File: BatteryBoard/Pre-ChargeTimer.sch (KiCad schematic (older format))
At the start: 9 parts

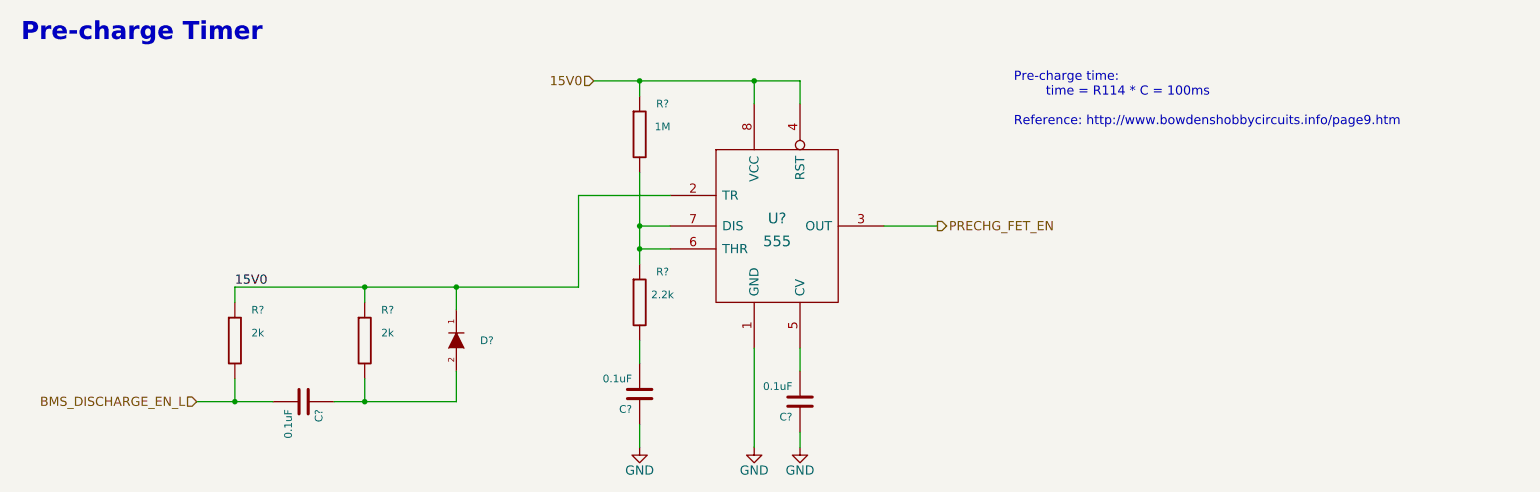
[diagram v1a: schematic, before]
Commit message: Added footprints for most components; started layout
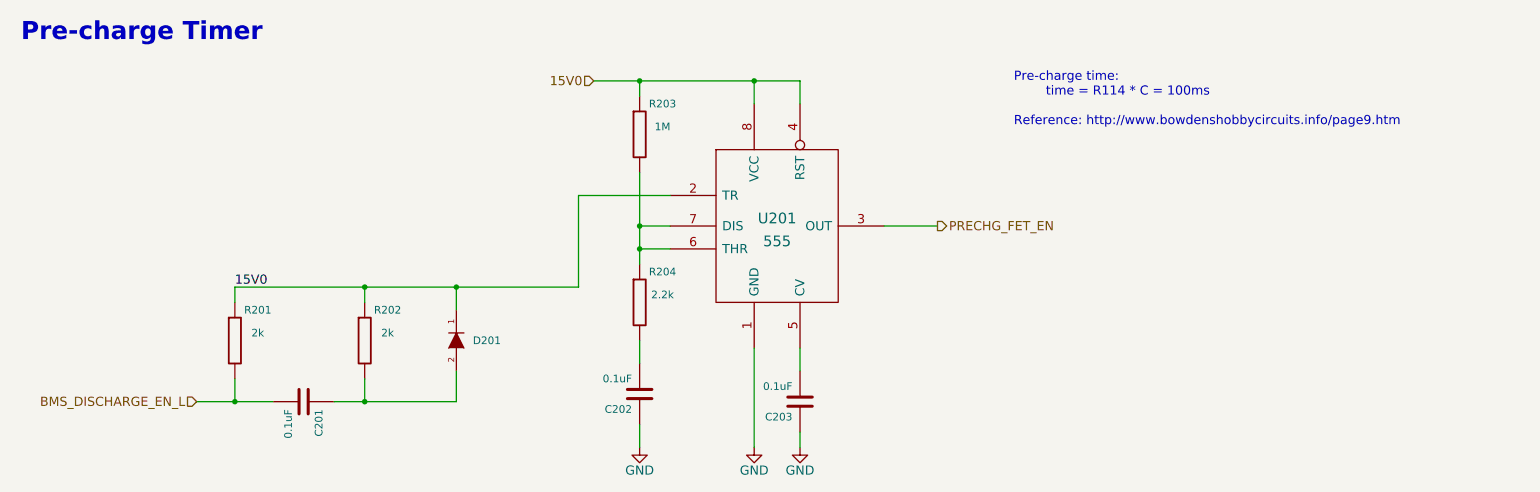
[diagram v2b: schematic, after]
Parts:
- C201, C202, C203: renamed from C?; footprint (none) -> Capacitors_SMD:C_0805_HandSoldering
- D201: renamed from D?; footprint (none) -> Diodes_SMD:D_SOD-523; Digi-Key PN (none) -> 1N4148XTPMSCT-ND; Mfg. (none) -> Micro; Mfg. PN (none) -> 1N4148X-TP
- R201, R202, R203, R204: renamed from R?; footprint (none) -> Resistors_SMD:R_0805_HandSoldering
- U201: renamed from U?; footprint (none) -> Housings_SOIC:SOIC-8_3.9x4.9mm_Pitch1.27mm; Digi-Key PN (none) -> 296-14635-1-ND; Mfg. (none) -> Texas Instruments; Mfg. PN (none) -> SA555DR
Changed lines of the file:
@@
 LIBS:xilinx
 LIBS:555
-LIBS:lt3014b
+LIBS:lt3060
+LIBS:lm321_5pin
 LIBS:BatteryBoard-cache
 EELAYER 25 0
@@
 Pre-charge time:\n		time = R114 * C = 100ms\n\nReference: http://www.bowdenshobbycircuits.info/page9.htm
 $Comp
-L R R?
+L R R201
 U 1 1 59655F30
 P 2050 2750
-F 0 "R?" H 2200 2950 50  0000 C CNN
+F 0 "R201" H 2200 2950 50  0000 C CNN
 F 1 "2k" H 2200 2800 50  0000 C CNN
-F 2 "" V 1980 2750 30  0000 C CNN
+F 2 "Resistors_SMD:R_0805_HandSoldering" V 1980 2750 30  0001 C CNN
 F 3 "" H 2050 2750 30  0000 C CNN
 	1    2050 2750
@@
 15V0
 $Comp
-L C C?
+L C C201
 U 1 1 59655F3C
 P 2500 3150
-F 0 "C?" H 2550 3250 50  0000 L CNN
+F 0 "C201" H 2550 3250 50  0000 L CNN
 F 1 "0.1uF" H 2550 3050 50  0000 L CNN
-F 2 "" H 2538 3000 30  0000 C CNN
+F 2 "Capacitors_SMD:C_0805_HandSoldering" H 2538 3000 30  0001 C CNN
 F 3 "" H 2500 3150 60  0000 C CNN
 	1    2500 3150
@@
 	2700 3150 3500 3150
 $Comp
-L R R?
+L R R202
 U 1 1 59655F45
 P 2900 2750
-F 0 "R?" H 3050 2950 50  0000 C CNN
+F 0 "R202" H 3050 2950 50  0000 C CNN
 F 1 "2k" H 3050 2800 50  0000 C CNN
-F 2 "" V 2830 2750 30  0000 C CNN
+F 2 "Resistors_SMD:R_0805_HandSoldering" V 2830 2750 30  0001 C CNN
 F 3 "" H 2900 2750 30  0000 C CNN
 	1    2900 2750
@@
 $EndComp
 $Comp
-L DIODE D?
+L DIODE D201
 U 1 1 59655F4C
 P 3500 2750
-F 0 "D?" V 3500 2950 50  0000 C CNN
+F 0 "D201" V 3500 2950 50  0000 C CNN
 F 1 "DIODE" H 3500 2650 50  0001 C CNN
-F 2 "" H 3500 2750 60  0000 C CNN
+F 2 "Diodes_SMD:D_SOD-523" H 3500 2750 60  0001 C CNN
 F 3 "" H 3500 2750 60  0000 C CNN
+F 4 "Micro" V 3500 2750 60  0001 C CNN "Mfg."
+F 5 "1N4148X-TP" V 3500 2750 60  0001 C CNN "Mfg. PN"
+F 6 "1N4148XTPMSCT-ND" V 3500 2750 60  0001 C CNN "Digi-Key PN"
 	1    3500 2750
 	0    1    -1   0
@@
 Connection ~ 5450 1050
 $Comp
-L C C?
+L C C203
 U 1 1 59655F5C
 P 5750 3150
-F 0 "C?" H 5800 3250 50  0000 L CNN
+F 0 "C203" H 5800 3250 50  0000 L CNN
 F 1 "0.1uF" H 5800 3050 50  0000 L CNN
-F 2 "" H 5788 3000 30  0000 C CNN
+F 2 "Capacitors_SMD:C_0805_HandSoldering" H 5788 3000 30  0001 C CNN
 F 3 "" H 5750 3150 60  0000 C CNN
 	1    5750 3150
@@
 	5750 3350 5750 3450
 $Comp
-L GND #PWR?
+L GND #PWR203
 U 1 1 59655F65
 P 5750 3450
-F 0 "#PWR?" H 5750 3200 60  0001 C CNN
+F 0 "#PWR203" H 5750 3200 60  0001 C CNN
 F 1 "GND" H 5750 3300 60  0000 C CNN
 F 2 "" H 5750 3450 60  0000 C CNN
@@
 	5450 2800 5450 3450
 $Comp
-L GND #PWR?
+L GND #PWR202
 U 1 1 59655F6C
 P 5450 3450
-F 0 "#PWR?" H 5450 3200 60  0001 C CNN
+F 0 "#PWR202" H 5450 3200 60  0001 C CNN
 F 1 "GND" H 5450 3300 60  0000 C CNN
 F 2 "" H 5450 3450 60  0000 C CNN
@@
 $EndComp
 $Comp
-L R R?
+L R R203
 U 1 1 59655F72
 P 4700 1400
-F 0 "R?" H 4850 1600 50  0000 C CNN
+F 0 "R203" H 4850 1600 50  0000 C CNN
 F 1 "1M" H 4850 1450 50  0000 C CNN
-F 2 "" V 4630 1400 30  0000 C CNN
+F 2 "Resistors_SMD:R_0805_HandSoldering" V 4630 1400 30  0001 C CNN
 F 3 "" H 4700 1400 30  0000 C CNN
 	1    4700 1400
@@
 Connection ~ 4700 2150
 $Comp
-L R R?
+L R R204
 U 1 1 59655F81
 P 4700 2500
-F 0 "R?" H 4850 2700 50  0000 C CNN
+F 0 "R204" H 4850 2700 50  0000 C CNN
 F 1 "2.2k" H 4850 2550 50  0000 C CNN
-F 2 "" V 4630 2500 30  0000 C CNN
+F 2 "Resistors_SMD:R_0805_HandSoldering" V 4630 2500 30  0001 C CNN
 F 3 "" H 4700 2500 30  0000 C CNN
 	1    4700 2500
@@
 $EndComp
 $Comp
-L C C?
+L C C202
 U 1 1 59655F88
 P 4700 3100
-F 0 "C?" H 4750 3200 50  0000 L CNN
+F 0 "C202" H 4750 3200 50  0000 L CNN
 F 1 "0.1uF" H 4750 3000 50  0000 L CNN
-F 2 "" H 4738 2950 30  0000 C CNN
+F 2 "Capacitors_SMD:C_0805_HandSoldering" H 4738 2950 30  0001 C CNN
 F 3 "" H 4700 3100 60  0000 C CNN
 	1    4700 3100
@@
 	4700 3300 4700 3450
 $Comp
-L GND #PWR?
+L GND #PWR201
 U 1 1 59655F91
 P 4700 3450
-F 0 "#PWR?" H 4700 3200 60  0001 C CNN
+F 0 "#PWR201" H 4700 3200 60  0001 C CNN
 F 1 "GND" H 4700 3300 60  0000 C CNN
 F 2 "" H 4700 3450 60  0000 C CNN
@@
 	3500 3150 3500 2950
 $Comp
-L 555 U?
+L 555 U201
 U 1 1 59655F28
 P 5600 2000
-F 0 "U?" H 5600 2050 70  0000 C CNN
+F 0 "U201" H 5600 2050 70  0000 C CNN
 F 1 "555" H 5600 1900 70  0000 C CNN
-F 2 "" H 5600 2000 60  0000 C CNN
+F 2 "Housings_SOIC:SOIC-8_3.9x4.9mm_Pitch1.27mm" H 5600 2000 60  0001 C CNN
 F 3 "" H 5600 2000 60  0000 C CNN
+F 4 "Texas Instruments" H 5600 2000 60  0001 C CNN "Mfg."
+F 5 "SA555DR" H 5600 2000 60  0001 C CNN "Mfg. PN"
+F 6 "296-14635-1-ND" H 5600 2000 60  0001 C CNN "Digi-Key PN"
 	1    5600 2000
 	1    0    0    -1

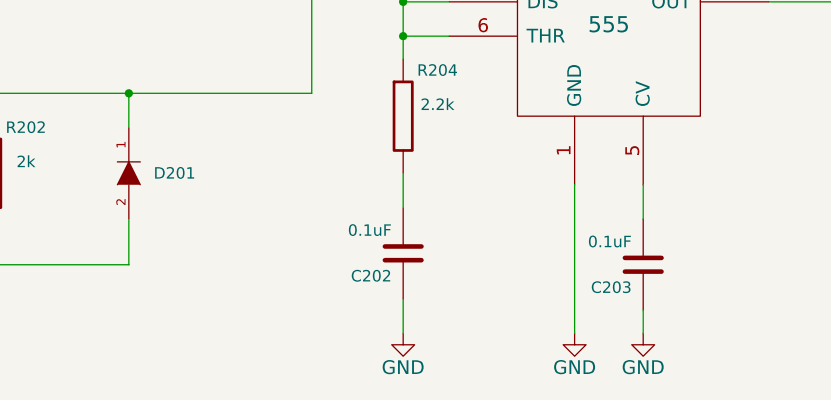
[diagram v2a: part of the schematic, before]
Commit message: Finished adding footprints; roughly placed all components
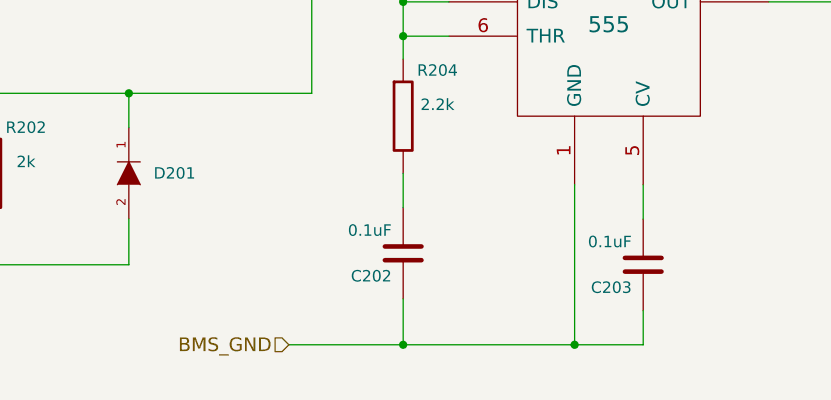
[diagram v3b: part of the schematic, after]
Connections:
- net GND renamed BMS_GND
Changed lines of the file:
@@
 LIBS:lt3060
 LIBS:lm321_5pin
+LIBS:AOB290L_nfet
 LIBS:BatteryBoard-cache
 EELAYER 25 0
@@
 	5750 2950 5750 2800
 Wire Wire Line
-	5750 3350 5750 3450
-$Comp
-L GND #PWR203
-U 1 1 59655F65
-P 5750 3450
-F 0 "#PWR203" H 5750 3200 60  0001 C CNN
-F 1 "GND" H 5750 3300 60  0000 C CNN
-F 2 "" H 5750 3450 60  0000 C CNN
-F 3 "" H 5750 3450 60  0000 C CNN
-	1    5750 3450
-	1    0    0    -1
-$EndComp
+	5750 3500 5750 3350
 Wire Wire Line
-	5450 2800 5450 3450
-$Comp
-L GND #PWR202
-U 1 1 59655F6C
-P 5450 3450
-F 0 "#PWR202" H 5450 3200 60  0001 C CNN
-F 1 "GND" H 5450 3300 60  0000 C CNN
-F 2 "" H 5450 3450 60  0000 C CNN
-F 3 "" H 5450 3450 60  0000 C CNN
-	1    5450 3450
-	1    0    0    -1
-$EndComp
+	5450 3500 5450 2800
 $Comp
 L R R203
@@
 	4700 2900 4700 2750
 Wire Wire Line
-	4700 3300 4700 3450
-$Comp
-L GND #PWR201
-U 1 1 59655F91
-P 4700 3450
-F 0 "#PWR201" H 4700 3200 60  0001 C CNN
-F 1 "GND" H 4700 3300 60  0000 C CNN
-F 2 "" H 4700 3450 60  0000 C CNN
-F 3 "" H 4700 3450 60  0000 C CNN
-	1    4700 3450
-	1    0    0    -1
-$EndComp
+	4700 3300 4700 3500
 Wire Wire Line
 	3500 2550 3500 2400
@@
 Wire Wire Line
 	6300 2000 6650 2000
+Text HLabel 4200 3500 0    60   Input ~ 0
+BMS_GND
+Wire Wire Line
+	4200 3500 5750 3500
+Connection ~ 4700 3500
+Connection ~ 5450 3500
 $EndSCHEMATC

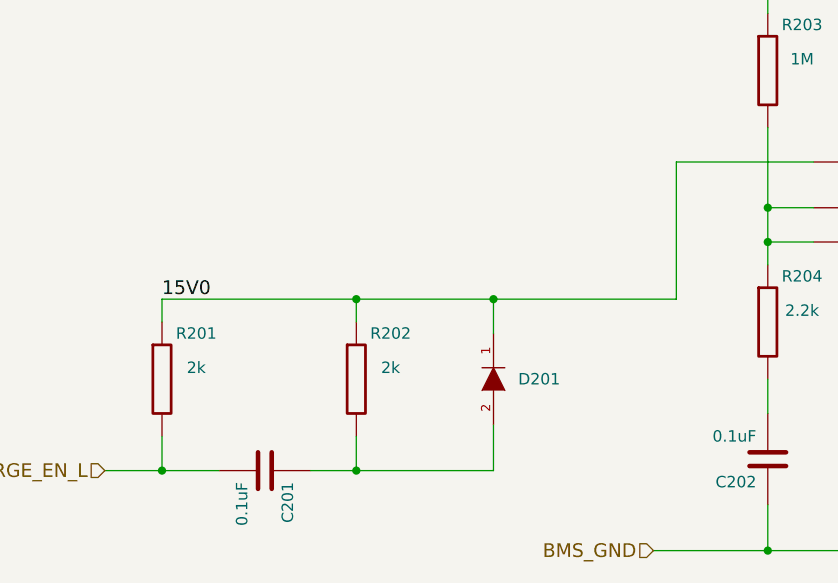
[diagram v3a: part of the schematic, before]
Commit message: Completed layout first pass - ready for review (pending validation w/ simulation)
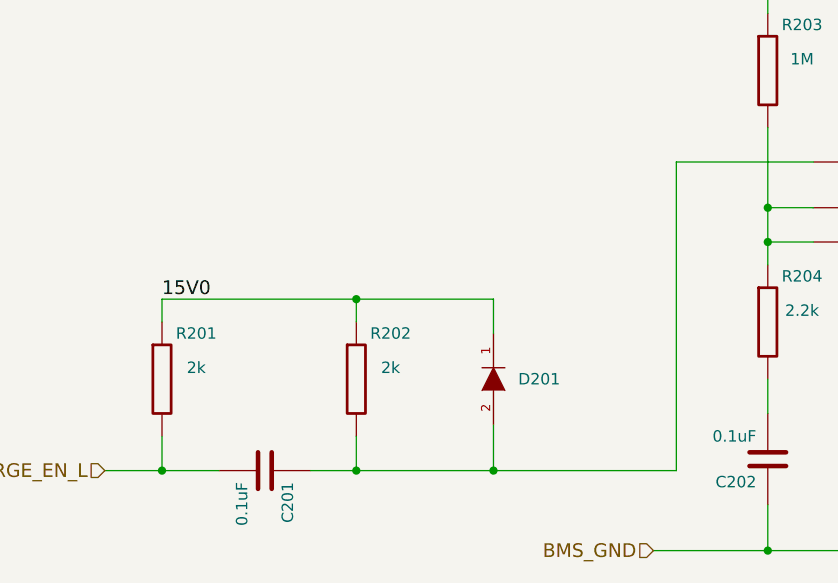
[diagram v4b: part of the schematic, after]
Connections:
- net 15V0: no longer U201.2 (TR)
- net at C201.1, D201.2 (A), R202.2: now also U201.2 (TR)
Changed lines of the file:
@@
 Wire Wire Line
 	2050 2500 2050 2400
-Wire Wire Line
-	2050 2400 4300 2400
 Text Label 2050 2400 0    60   ~ 0
 15V0
@@
 Connection ~ 2050 3150
 Wire Wire Line
-	2700 3150 3500 3150
+	4300 3150 2700 3150
 $Comp
 L R R202
@@
 Connection ~ 4700 2000
 Wire Wire Line
-	4300 2400 4300 1800
+	4300 1800 4300 3150
 Wire Wire Line
 	4300 1800 4900 1800
@@
 Wire Wire Line
 	3500 2550 3500 2400
-Connection ~ 3500 2400
 Wire Wire Line
 	3500 3150 3500 2950
@@
 Connection ~ 4700 3500
 Connection ~ 5450 3500
+Connection ~ 3500 3150
+Wire Wire Line
+	3500 2400 2050 2400
 $EndSCHEMATC

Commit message: Updated silkscreen; optimized current consumption; added subcircuit simulations
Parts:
- U201: Digi-Key PN 296-14635-1-ND -> LMC555CMX/NOPBCT-ND; Mfg. PN SA555DR -> LMC555CMX/NOPB
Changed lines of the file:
@@
 F 3 "" H 5600 2000 60  0000 C CNN
 F 4 "Texas Instruments" H 5600 2000 60  0001 C CNN "Mfg."
-F 5 "SA555DR" H 5600 2000 60  0001 C CNN "Mfg. PN"
-F 6 "296-14635-1-ND" H 5600 2000 60  0001 C CNN "Digi-Key PN"
+F 5 "LMC555CMX/NOPB" H 5600 2000 60  0001 C CNN "Mfg. PN"
+F 6 "LMC555CMX/NOPBCT-ND" H 5600 2000 60  0001 C CNN "Digi-Key PN"
 	1    5600 2000
 	1    0    0    -1

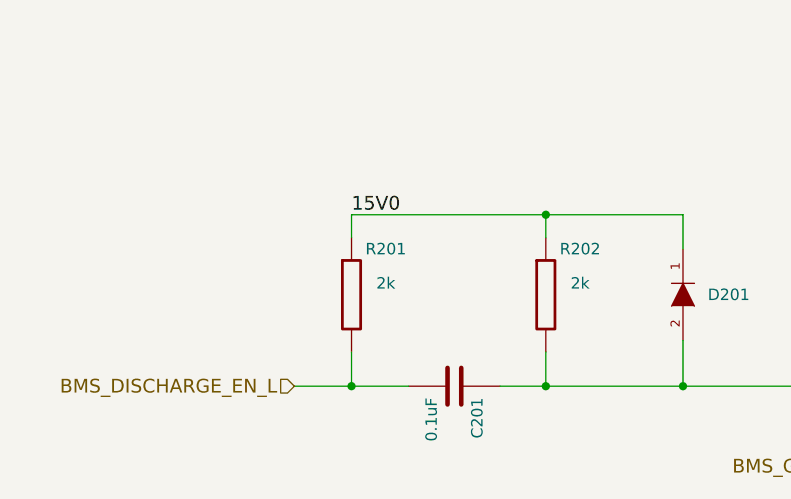
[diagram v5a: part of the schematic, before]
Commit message: Updated 555 timer to CMOS version
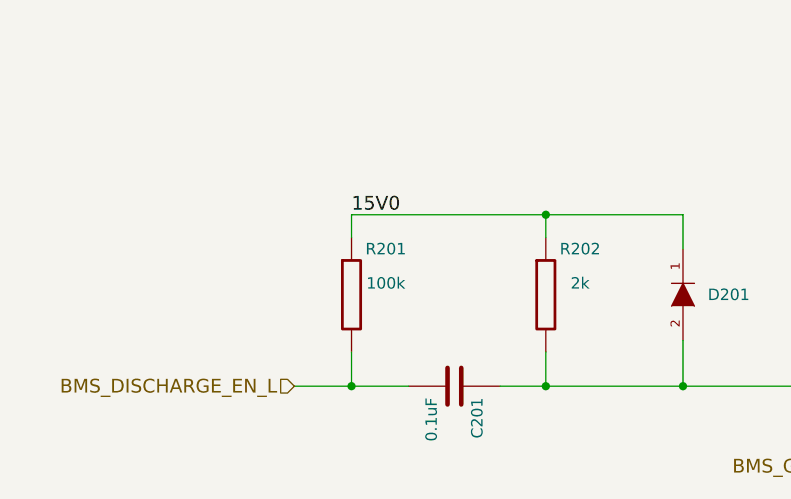
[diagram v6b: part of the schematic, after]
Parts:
- R201: value 2k -> 100k
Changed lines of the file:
@@
 P 2050 2750
 F 0 "R201" H 2200 2950 50  0000 C CNN
-F 1 "2k" H 2200 2800 50  0000 C CNN
+F 1 "100k" H 2200 2800 50  0000 C CNN
 F 2 "Resistors_SMD:R_0805_HandSoldering" V 1980 2750 30  0001 C CNN
 F 3 "" H 2050 2750 30  0000 C CNN
